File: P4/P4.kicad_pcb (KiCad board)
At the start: 2 copper layers, 65 x 56 mm, 16 parts, among them J1 RPi_GPIO, U1 PGA2310

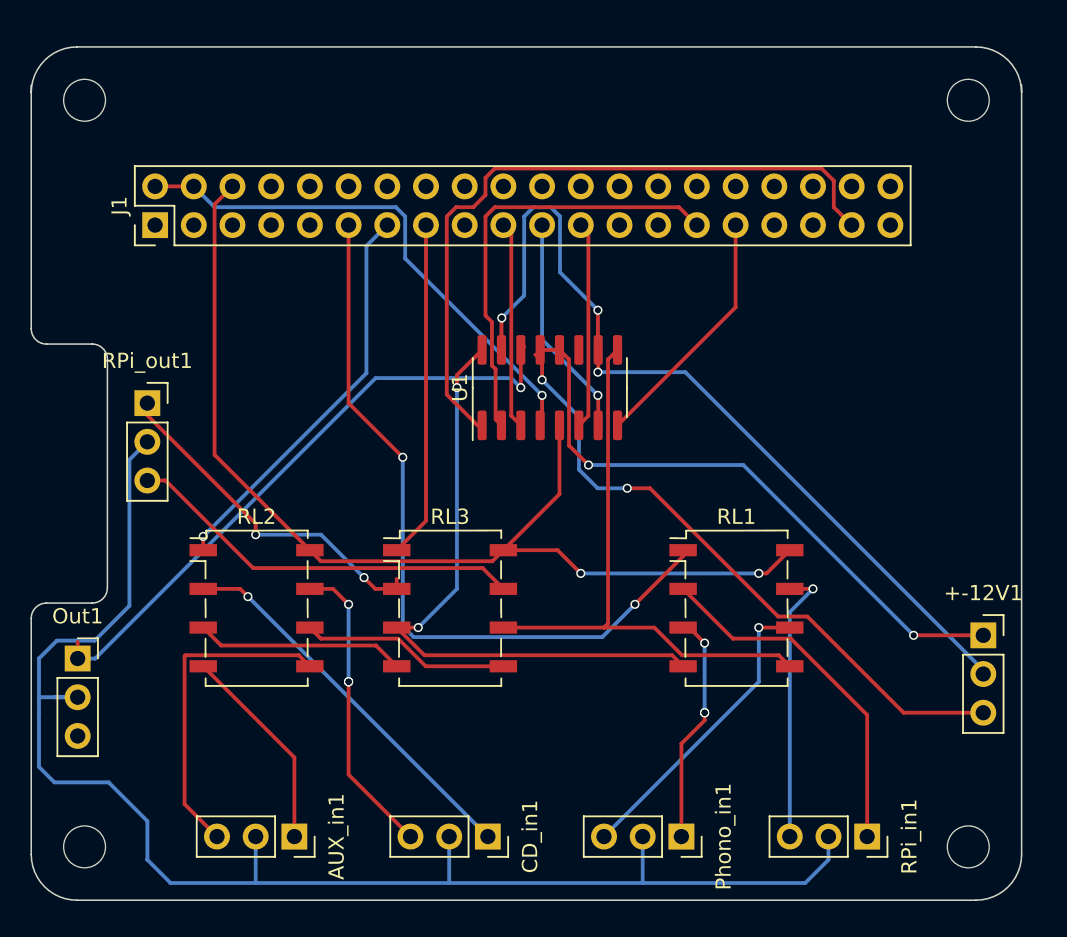
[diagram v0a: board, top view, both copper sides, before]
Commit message: Add connections for rotary encoder, display and power relay
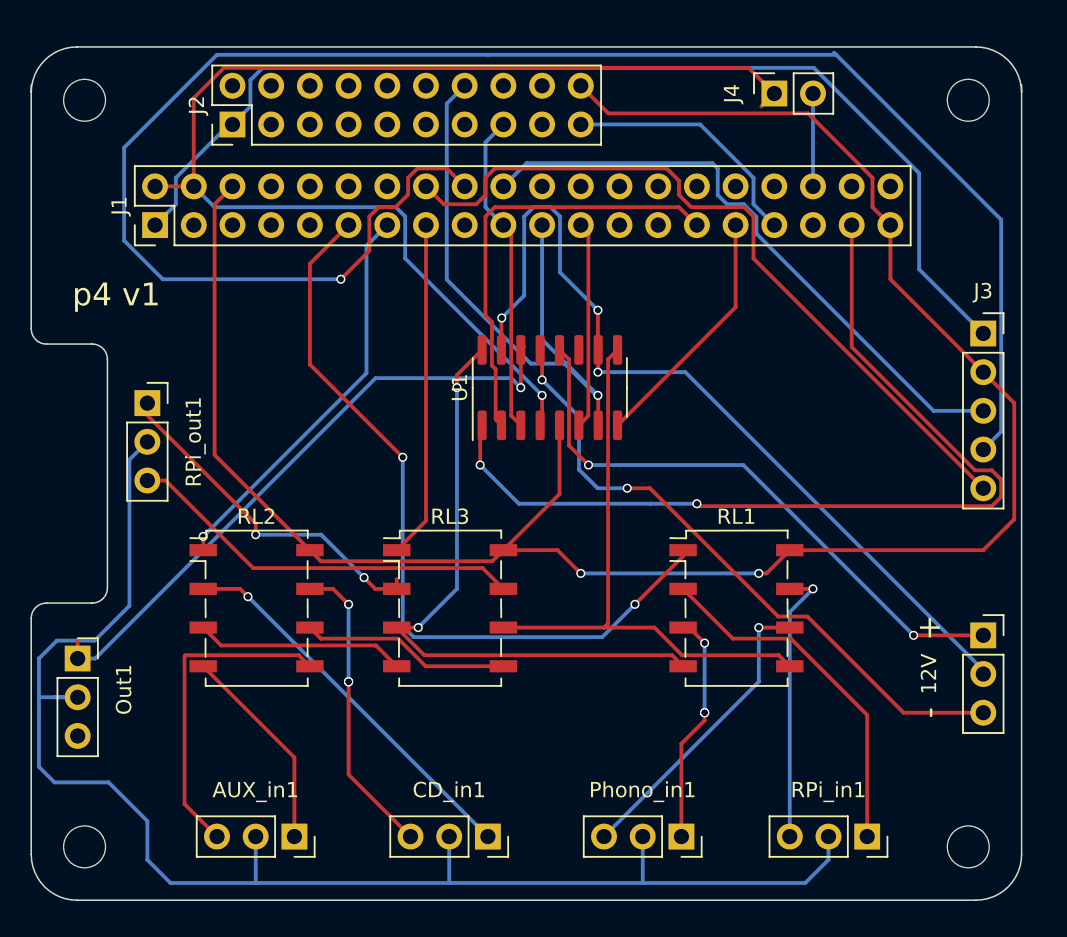
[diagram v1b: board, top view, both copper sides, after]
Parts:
- added J2: Conn_02x10_Odd_Even, Connector_PinHeader_2.54mm:PinHeader_2x10_P2.54mm_Vertical, F.Cu at (98.6, 87.9)
- added J3: Conn_01x05_Male, Connector_PinSocket_2.54mm:PinSocket_1x05_P2.54mm_Vertical, F.Cu at (147.8, 101.6)
- added J4: Conn_01x02_Male, Connector_PinSocket_2.54mm:PinSocket_1x02_P2.54mm_Vertical, F.Cu at (134.1, 85.9)
- renumbered +-12V1 to 12V
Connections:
- J1 pad 1: (no net) -> +3V3
- J1 pad 16: (no net) -> Net-(J1-Pad16)
- J1 pad 18: (no net) -> Net-(J1-Pad18)
- J1 pad 20: (no net) -> Net-(J1-Pad20)
- J1 pad 33: (no net) -> #EPD_CS
- J1 pad 36: (no net) -> Net-(J1-Pad36)
- J1 pad 39: (no net) -> GND
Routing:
- net Net-(J1-Pad18): track 0.00 -> 115.3 mm, vias 0 -> 1
- net +3V3: track 0.00 -> 71.6 mm
- net GND: track 70.0 -> 133.5 mm
- net Net-(J1-Pad16): track 0.00 -> 49.6 mm
- net +5V: track 34.7 -> 81.3 mm
- net Net-(J1-Pad20): track 0.00 -> 40.5 mm
- net MISO: track 14.7 -> 40.9 mm
- net #EPD_CS: track 0.00 -> 16.5 mm
- net ZCEN: track 45.9 -> 60.5 mm, vias 0 -> 2
- net MOSI: track 13.6 -> 21.2 mm
- net Net-(J1-Pad36): track 0.00 -> 6.10 mm
- net Net-(J1-Pad11): track 49.1 -> 51.2 mm
- net Net-(+-12V1-Pad1): track 40.2 -> 38.9 mm
- net Net-(+-12V1-Pad3): track 41.9 -> 41.2 mm
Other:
- board text added: "+"
- board text added: "-"
- board text added: "p4 v1"

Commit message: Add transistors for relays
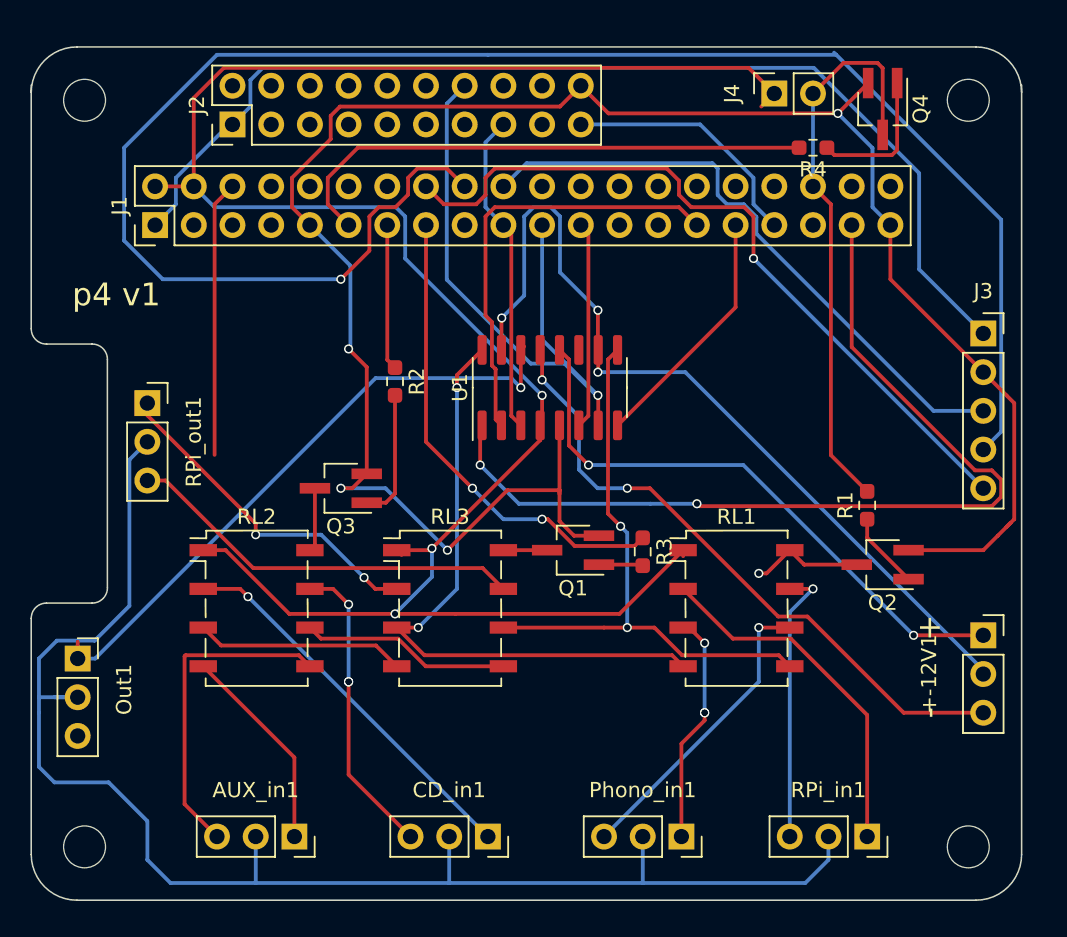
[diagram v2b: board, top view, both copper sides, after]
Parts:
- added Q1: Q_NPN_BEC, Package_TO_SOT_SMD:SOT-23W_Handsoldering, F.Cu at (120.9, 115.8)
- added Q2: Q_NPN_BEC, Package_TO_SOT_SMD:SOT-23W_Handsoldering, F.Cu at (141.2, 116.8)
- added Q3: Q_NPN_BEC, Package_TO_SOT_SMD:SOT-23W_Handsoldering, F.Cu at (105.7, 111.8)
- added Q4: Q_NPN_BEC, Package_TO_SOT_SMD:SOT-23W_Handsoldering, F.Cu at (141.2, 86.9)
- added R1: 1k, Resistor_SMD:R_0603_1608Metric_Pad0.98x0.95mm_HandSolder, F.Cu at (140.2, 112.9)
- added R2: 1k, Resistor_SMD:R_0603_1608Metric_Pad0.98x0.95mm_HandSolder, F.Cu at (109.2, 104.8)
- added R3: 1k, Resistor_SMD:R_0603_1608Metric_Pad0.98x0.95mm_HandSolder, F.Cu at (125.5, 115.9)
- added R4: 1k, Resistor_SMD:R_0603_1608Metric_Pad0.98x0.95mm_HandSolder, F.Cu at (136.7, 89.4)
- renumbered 12V to +-12V1
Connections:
- J1 pad 11: Net-(J1-Pad11) -> RL4
- J1 pad 13: Net-(J1-Pad13) -> RL2
- J1 pad 15: Net-(J1-Pad15) -> RL3
- J1 pad 36: Net-(J1-Pad36) -> RL1
- J1 pad 6: GND -> (no net)
- J1 pad 9: (no net) -> GND
- J4 pad 2: Net-(J1-Pad36) -> Net-(J4-Pad2)
- RL1 pad 1: Net-(J1-Pad11) -> +5V
- RL1 pad 8: GND -> Net-(Q2-Pad3)
- RL2 pad 1: Net-(J1-Pad13) -> +5V
- RL2 pad 8: GND -> Net-(Q3-Pad3)
- RL3 pad 1: Net-(J1-Pad15) -> +5V
- RL3 pad 8: GND -> Net-(Q1-Pad3)
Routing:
- net +5V: track 81.3 -> 135.2 mm, vias 1 -> 3
- net Net-(J1-Pad11): track 51.2 -> 0.00 mm, vias 2 -> 0
- net RL4: track 0.00 -> 35.4 mm
- net RL3: track 0.00 -> 31.5 mm, vias 0 -> 2
- net Net-(J1-Pad13): track 26.3 -> 0.00 mm, vias 2 -> 0
- net Net-(J1-Pad15): track 22.1 -> 0.00 mm
- net RL1: track 0.00 -> 21.5 mm
- net (no net): track 0.00 -> 18.1 mm
- net Net-(J4-Pad2): track 0.00 -> 9.93 mm
- net RL2: track 0.00 -> 9.56 mm
- net Net-(Q4-Pad1): track 0.00 -> 9.34 mm
- net Net-(Q3-Pad1): track 0.00 -> 8.55 mm
- net Net-(Q2-Pad3): track 0.00 -> 7.45 mm, vias 0 -> 1
- net Net-(Q2-Pad1): track 0.00 -> 5.06 mm
- net Net-(Q3-Pad3): track 0.00 -> 4.20 mm
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
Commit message: Guarduino switched to MCP3008, PCB not done
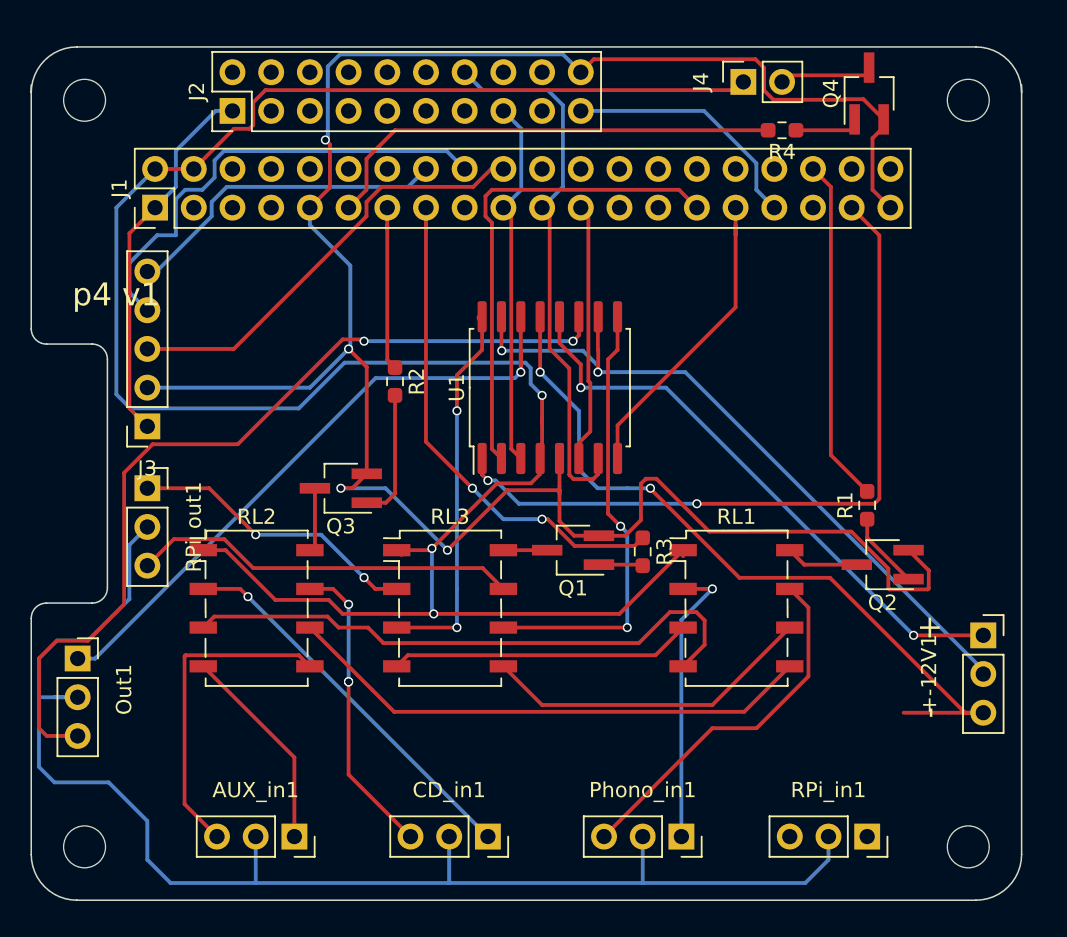
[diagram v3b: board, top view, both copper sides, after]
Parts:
- U1: footprint Package_SO:SOIC-16_3.9x9.9mm_P1.27mm -> Package_SO:SOIC-16W_7.5x10.3mm_P1.27mm
- moved J3 55.2 mm to (93.0, 107.7), turned to 180 degrees
- moved RPi_out1 5.59 mm to (93.0, 111.8)
- moved R4 2.33 mm to (134.6, 88.3)
- moved J4 2.17 mm to (132.1, 85.1)
- moved Q4 1.35 mm to (140.3, 85.9), turned to 90 degrees
- moved J1 1.14 mm to (93.5, 93.3)
- moved J2 0.89 mm to (98.6, 87.0)
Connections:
- net Net-(Out1-Pad1) renamed /OutL
- Out1 pad 3: (no net) -> /OutR
- RL1 pad 2: /RPi_in_L -> /Phono_in_L
- RL1 pad 3: /Phono_in_L -> /INL
- RL1 pad 4: INL -> /CD|Aux_L
- RL1 pad 5: INR -> /CD|Aux_R
- RL1 pad 6: /Phono_in_R -> /INR
- RL1 pad 7: /RPi_in_R -> /Phono_in_R
- RL2 pad 3: Net-(RL2-Pad3) -> /CD|Aux_L
- RL2 pad 6: Net-(RL2-Pad6) -> /CD|Aux_R
- RL3 pad 3: INL -> /VCL
- RL3 pad 4: Net-(RL2-Pad3) -> /INL
- RL3 pad 5: Net-(RL2-Pad6) -> /INR
- RL3 pad 6: INR -> /VCR
- RPi_in1 pad 1: /RPi_in_L -> (no net)
- RPi_in1 pad 3: /RPi_in_R -> (no net)
- U1 pad 11: (no net) -> /OutR
- U1 pad 16: INL -> /VCL
- U1 pad 9: INR -> /VCR
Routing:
- net Net-(J1-Pad18): track 115.3 -> 31.2 mm, vias 1 -> 0
- net /OutR: track 0.00 -> 57.9 mm, vias 0 -> 2
- net +3V3: track 71.6 -> 24.6 mm
- net INL: track 41.2 -> 0.00 mm, vias 2 -> 0
- net INR: track 38.9 -> 0.00 mm, vias 2 -> 0
- net /CD|Aux_L: track 0.00 -> 38.6 mm
- net /CD|Aux_R: track 0.00 -> 35.0 mm
- net /VCR: track 0.00 -> 29.3 mm, vias 0 -> 2
- net Net-(J1-Pad16): track 49.6 -> 21.6 mm, vias 1 -> 0
- net /VCL: track 0.00 -> 25.1 mm, vias 0 -> 2
- net /RPi_in_L: track 23.5 -> 0.00 mm
- net /INR: track 0.00 -> 22.0 mm
- net /INL: track 0.00 -> 20.2 mm
- net /RPi_in_R: track 18.4 -> 0.00 mm, vias 1 -> 0
- net (no net): track 18.1 -> 0.00 mm
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
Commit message: Updates for Kicad 8, different output wiring
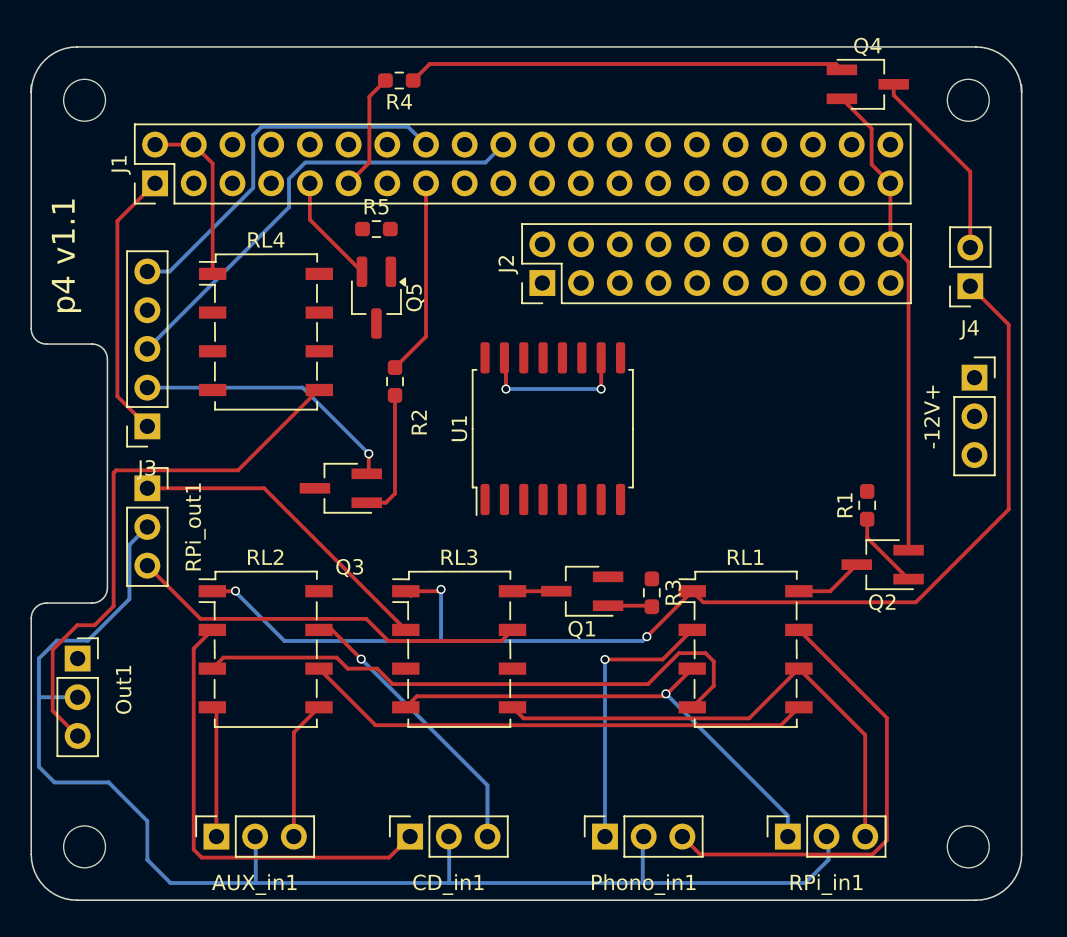
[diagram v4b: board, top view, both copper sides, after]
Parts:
- added Q5: Q_NPN_BEC, Package_TO_SOT_SMD:SOT-23W_Handsoldering, F.Cu at (108.0, 99.2)
- added R5: 1k, Resistor_SMD:R_0603_1608Metric_Pad0.98x0.95mm_HandSolder, F.Cu at (108.0, 94.8)
- added RL4: Omron_G6K, Relay_SMD:Relay_DPDT_Omron_G6K-2F, F.Cu at (100.8, 101.5)
- moved R4 25.3 mm to (109.5, 85.0)
- moved J2 23.3 mm to (118.9, 98.3)
- moved J4 20.0 mm to (147.0, 98.5), turned to 180 degrees
- moved -12V+ 16.9 mm to (147.2, 104.5)
- moved RPi_in1 5.21 mm to (135.0, 134.6), turned to 90 degrees
- moved AUX_in1 5.12 mm to (97.5, 134.6), turned to 90 degrees
- moved CD_in1 5.11 mm to (110.2, 134.6), turned to 90 degrees
- moved Phono_in1 5.02 mm to (123.0, 134.6), turned to 90 degrees
- moved RL1 2.76 mm to (132.2, 122.3)
- moved Q1 2.76 mm to (121.5, 118.5)
- moved RL3 2.76 mm to (113.4, 122.3)
- moved R3 2.76 mm to (126.1, 118.6)
- moved RL2 2.76 mm to (100.7, 122.3)
- moved U1 2.70 mm to (119.6, 107.8)
- moved J1 1.60 mm to (93.5, 91.7)
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- renumbered +-12V1 to -12V+
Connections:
- net +3V3 renamed +3.3V
- net Net-(+-12V1-Pad1) renamed +12V
- net Net-(+-12V1-Pad3) renamed -12V
- J1 pad 10: (no net) -> unconnected-(J1-BCM15_RXD-Pad10)
- J1 pad 12: (no net) -> unconnected-(J1-BCM18_PCM_C-Pad12)
- J1 pad 14: (no net) -> unconnected-(J1-GND-Pad14)
- J1 pad 17: (no net) -> unconnected-(J1-3.3V-Pad17)
- J1 pad 22: (no net) -> RL1
- J1 pad 24: (no net) -> unconnected-(J1-BCM8_CE0-Pad24)
- J1 pad 25: (no net) -> unconnected-(J1-GND-Pad25)
- J1 pad 26: (no net) -> unconnected-(J1-BCM7_CE1-Pad26)
- J1 pad 27: (no net) -> unconnected-(J1-BCM0_ID_SD-Pad27)
- J1 pad 28: (no net) -> unconnected-(J1-BCM1_ID_SC-Pad28)
- J1 pad 3: (no net) -> unconnected-(J1-BCM2_SDA-Pad3)
- J1 pad 30: (no net) -> unconnected-(J1-GND-Pad30)
- J1 pad 32: (no net) -> unconnected-(J1-BCM12_PWM0-Pad32)
- J1 pad 34: (no net) -> unconnected-(J1-GND-Pad34)
- J1 pad 35: (no net) -> unconnected-(J1-BCM19_MISO_PCM_FS-Pad35)
- J1 pad 38: (no net) -> unconnected-(J1-BCM20_MOSI_PCM_DI-Pad38)
- J1 pad 40: (no net) -> unconnected-(J1-BCM21_SCLK_PCM_DO-Pad40)
- J1 pad 5: (no net) -> unconnected-(J1-BCM3_SCL-Pad5)
- J1 pad 6: (no net) -> unconnected-(J1-GND-Pad6)
- J1 pad 7: (no net) -> unconnected-(J1-BCM4_GPCLK0-Pad7)
- J1 pad 8: (no net) -> unconnected-(J1-BCM14_TXD-Pad8)
- J2 pad 10: (no net) -> unconnected-(J2-Pin_10-Pad10)
- J2 pad 11: (no net) -> unconnected-(J2-Pin_11-Pad11)
- J2 pad 12: (no net) -> unconnected-(J2-Pin_12-Pad12)
- J2 pad 13: (no net) -> unconnected-(J2-Pin_13-Pad13)
- J2 pad 16: (no net) -> unconnected-(J2-Pin_16-Pad16)
- J2 pad 17: (no net) -> unconnected-(J2-Pin_17-Pad17)
- J2 pad 18: (no net) -> unconnected-(J2-Pin_18-Pad18)
- J2 pad 2: (no net) -> unconnected-(J2-Pin_2-Pad2)
- J2 pad 3: (no net) -> unconnected-(J2-Pin_3-Pad3)
- J2 pad 4: (no net) -> unconnected-(J2-Pin_4-Pad4)
- J2 pad 5: (no net) -> unconnected-(J2-Pin_5-Pad5)
- J2 pad 6: (no net) -> unconnected-(J2-Pin_6-Pad6)
- J2 pad 7: (no net) -> unconnected-(J2-Pin_7-Pad7)
- J2 pad 8: (no net) -> unconnected-(J2-Pin_8-Pad8)
- J2 pad 9: (no net) -> unconnected-(J2-Pin_9-Pad9)
- R1 pad 2: RL1 -> RL2
- R2 pad 1: RL2 -> RL3
- R3 pad 1: RL3 -> RL4
- RPi_in1 pad 1: (no net) -> /INL
- RPi_in1 pad 3: (no net) -> /INR
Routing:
- net GND: track 148.8 -> 56.1 mm, vias 4 -> 1
- net +5V: track 145.3 -> 90.6 mm
- net -12V: track 49.5 -> 0.00 mm, vias 2 -> 0
- net ZCEN: track 48.5 -> 0.00 mm, vias 2 -> 0
- net /OutL: track 41.7 -> 0.00 mm, vias 1 -> 0
- net +12V: track 38.4 -> 0.00 mm, vias 2 -> 0
- net MISO: track 37.2 -> 0.00 mm
- net Net-(+-12V1-Pin_2): track 47.2 -> 10.5 mm
- net #CS: track 32.2 -> 0.00 mm
- net Net-(J1-BCM24): track 31.2 -> 0.00 mm
- net /VCR: track 29.3 -> 0.00 mm, vias 2 -> 0
- net /VCL: track 25.1 -> 0.00 mm, vias 2 -> 0
- net Net-(Q4-B): track 3.94 -> 28.7 mm
- net MOSI: track 24.3 -> 0.00 mm
- net RL4: track 30.8 -> 7.75 mm
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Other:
- net class Default removed
- board text added: "p4 v1.1"
- board text removed: "+"
- board text removed: "-"
- board text removed: "p4 v1"
